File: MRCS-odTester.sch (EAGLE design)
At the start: 14 parts

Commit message: 1.1
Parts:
- added DCC, TRACK: (no value), SPCoast:CONNECTOR-M02508-LOCK
- R1: value 15k -> 100k
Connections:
- removed net TRACK+: DCCOD-2.S, SW1.S, SW1.S1, SW2.S, SW2.S1, SW3.S, SW3.S1
- removed net TRACK-: DCCOD-4.S, R1.1, R2.1, R3.1
- new net DCC-COMMON: DCC.2, DCCOD-4.S
- new net DCC-FROMTRACK: DCCOD-2.S, SW1.S, SW1.S1, SW2.S, SW2.S1, SW3.S, SW3.S1, TRACK.1
- new net DCC-TOTRACK: DCC.1, R1.1, R2.1, R3.1, TRACK.2
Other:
- moved on the sheet: C1, C2, CON1, DCCOD-1, DCCOD-2, DCCOD-3, DCCOD-4, DCCOD-5, LED1, R1, R2, R3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

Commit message: 2.0
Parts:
- BOARD1: value BOARD50X50 -> (none)
- C1: device SPCoast:CAP-POLPTH-5MM -> SPCoast:CAP-POLPTH-3.5MM
- R1, R2, R3, R4: device SPCoast:RPTH1 -> SPCoast:RPTH04
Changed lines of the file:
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@@
 <grid distance="0.1" unitdist="inch" unit="inch" style="lines" multiple="1" display="no" altdistance="0.01" altunitdist="inch" altunit="inch"/>
 <layers>
-<layer number="1" name="Top" color="4" fill="1" visible="no" active="no"/>
-<layer number="2" name="Route2" color="1" fill="3" visible="no" active="no"/>
-<layer number="3" name="Route3" color="4" fill="3" visible="no" active="no"/>
-<layer number="14" name="Route14" color="1" fill="6" visible="no" active="no"/>
-<layer number="15" name="Route15" color="4" fill="6" visible="no" active="no"/>
-<layer number="16" name="Bottom" color="2" fill="1" visible="no" active="no"/>
-<layer number="17" name="Pads" color="2" fill="1" visible="no" active="no"/>
-<layer number="18" name="Vias" color="2" fill="1" visible="no" active="no"/>
-<layer number="19" name="Unrouted" color="6" fill="1" visible="no" active="no"/>
-<layer number="20" name="Dimension" color="27" fill="1" visible="no" active="no"/>
-<layer number="21" name="tPlace" color="20" fill="1" visible="no" active="no"/>
-<layer number="22" name="bPlace" color="7" fill="1" visible="no" active="no"/>
-<layer number="23" name="tOrigins" color="15" fill="1" visible="no" active="no"/>
-<layer number="24" name="bOrigins" color="15" fill="1" visible="no" active="no"/>
-<layer number="25" name="tNames" color="7" fill="1" visible="no" active="no"/>
-<layer number="26" name="bNames" color="7" fill="1" visible="no" active="no"/>
-<layer number="27" name="tValues" color="7" fill="1" visible="no" active="no"/>
-<layer number="28" name="bValues" color="7" fill="1" visible="no" active="no"/>
+<layer number="1" name="Top" color="4" fill="1" visible="yes" active="no"/>
+<layer number="2" name="Route2" color="1" fill="3" visible="yes" active="no"/>
+<layer number="3" name="Route3" color="4" fill="3" visible="yes" active="no"/>
+<layer number="14" name="Route14" color="1" fill="6" visible="yes" active="no"/>
+<layer number="15" name="Route15" color="4" fill="6" visible="yes" active="no"/>
+<layer number="16" name="Bottom" color="1" fill="1" visible="yes" active="no"/>
+<layer number="17" name="Pads" color="2" fill="1" visible="yes" active="no"/>
+<layer number="18" name="Vias" color="2" fill="1" visible="yes" active="no"/>
+<layer number="19" name="Unrouted" color="6" fill="1" visible="yes" active="no"/>
+<layer number="20" name="Dimension" color="15" fill="1" visible="yes" active="no"/>
+<layer number="21" name="tPlace" color="7" fill="1" visible="yes" active="no"/>
+<layer number="22" name="bPlace" color="7" fill="1" visible="yes" active="no"/>
+<layer number="23" name="tOrigins" color="15" fill="1" visible="yes" active="no"/>
+<layer number="24" name="bOrigins" color="15" fill="1" visible="yes" active="no"/>
+<layer number="25" name="tNames" color="7" fill="1" visible="yes" active="no"/>
+<layer number="26" name="bNames" color="7" fill="1" visible="yes" active="no"/>
+<layer number="27" name="tValues" color="7" fill="1" visible="yes" active="no"/>
+<layer number="28" name="bValues" color="7" fill="1" visible="yes" active="no"/>
 <layer number="29" name="tStop" color="7" fill="3" visible="no" active="no"/>
 <layer number="30" name="bStop" color="7" fill="6" visible="no" active="no"/>
@@
 <layer number="35" name="tGlue" color="7" fill="4" visible="no" active="no"/>
 <layer number="36" name="bGlue" color="7" fill="5" visible="no" active="no"/>
-<layer number="37" name="tTest" color="7" fill="1" visible="no" active="no"/>
-<layer number="38" name="bTest" color="7" fill="1" visible="no" active="no"/>
+<layer number="37" name="tTest" color="7" fill="1" visible="yes" active="no"/>
+<layer number="38" name="bTest" color="7" fill="1" visible="yes" active="no"/>
 <layer number="39" name="tKeepout" color="4" fill="11" visible="no" active="no"/>
 <layer number="40" name="bKeepout" color="1" fill="11" visible="no" active="no"/>
@@
 <layer number="44" name="Drills" color="7" fill="1" visible="no" active="no"/>
 <layer number="45" name="Holes" color="7" fill="1" visible="no" active="no"/>
-<layer number="46" name="Milling" color="3" fill="1" visible="no" active="no"/>
-<layer number="47" name="Measures" color="7" fill="1" visible="no" active="no"/>
-<layer number="48" name="Document" color="7" fill="1" visible="no" active="no"/>
-<layer number="49" name="Reference" color="21" fill="1" visible="no" active="no"/>
-<layer number="50" name="dxf" color="7" fill="1" visible="no" active="no"/>
-<layer number="51" name="tDocu" color="16" fill="1" visible="no" active="no"/>
-<layer number="52" name="bDocu" color="31" fill="1" visible="no" active="no"/>
-<layer number="53" name="tGND_GNDA" color="7" fill="9" visible="no" active="no"/>
-<layer number="54" name="bGND_GNDA" color="1" fill="9" visible="no" active="no"/>
-<layer number="56" name="wert" color="7" fill="1" visible="no" active="no"/>
-<layer number="57" name="tCAD" color="7" fill="1" visible="no" active="no"/>
-<layer number="59" name="tCarbon" color="7" fill="1" visible="no" active="no"/>
-<layer number="60" name="bCarbon" color="7" fill="1" visible="no" active="no"/>
+<layer number="46" name="Milling" color="3" fill="1" visible="yes" active="no"/>
+<layer number="47" name="Measures" color="7" fill="1" visible="yes" active="no"/>
+<layer number="48" name="Document" color="7" fill="1" visible="yes" active="no"/>
+<layer number="49" name="Reference" color="7" fill="1" visible="yes" active="no"/>
+<layer number="50" name="dxf" color="7" fill="1" visible="yes" active="no"/>
+<layer number="51" name="tDocu" color="7" fill="1" visible="yes" active="no"/>
+<layer number="52" name="bDocu" color="7" fill="1" visible="yes" active="no"/>
+<layer number="53" name="tGND_GNDA" color="7" fill="9" visible="yes" active="no"/>
+<layer number="54" name="bGND_GNDA" color="1" fill="9" visible="yes" active="no"/>
+<layer number="56" name="wert" color="7" fill="1" visible="yes" active="no"/>
+<layer number="57" name="tCAD" color="7" fill="1" visible="yes" active="no"/>
+<layer number="59" name="tCarbon" color="7" fill="1" visible="yes" active="no"/>
+<layer number="60" name="bCarbon" color="7" fill="1" visible="yes" active="no"/>
 <layer number="90" name="Modules" color="5" fill="1" visible="yes" active="yes"/>
 <layer number="91" name="Nets" color="2" fill="1" visible="yes" active="yes"/>
@@
 <part name="FRAME1" library="SPCoast" deviceset="DOC-FRAME-LETTER" device=""/>
 <part name="DCCOD" library="con-molex" deviceset="KK-156-5" device=""/>
-<part name="C1" library="SPCoast" deviceset="CAP-POL*" device="PTH-5MM" value="100uF"/>
+<part name="C1" library="SPCoast" deviceset="CAP-POL*" device="PTH-3.5MM" value="100uF"/>
 <part name="C2" library="SPCoast" deviceset="CAP*" device="" value="0.1uf"/>
-<part name="R1" library="SPCoast" deviceset="R*" device="PTH1" value="100k"/>
-<part name="R2" library="SPCoast" deviceset="R*" device="PTH1" value="10k"/>
-<part name="R3" library="SPCoast" deviceset="R*" device="PTH1" value="5k"/>
+<part name="R1" library="SPCoast" deviceset="R*" device="PTH04" value="100k"/>
+<part name="R2" library="SPCoast" deviceset="R*" device="PTH04" value="10k"/>
+<part name="R3" library="SPCoast" deviceset="R*" device="PTH04" value="5k"/>
 <part name="SW1" library="SPCoast" deviceset="SWITCH-10-XX" device=""/>
 <part name="SW2" library="SPCoast" deviceset="SWITCH-10-XX" device=""/>
@@
 <part name="P+1" library="supply1" deviceset="+12V" device=""/>
 <part name="CON1" library="SPCoast" deviceset="CONNECTOR-DC-POWER" device="-RA"/>
-<part name="R4" library="SPCoast" deviceset="R*" device="PTH1" value="2k"/>
+<part name="R4" library="SPCoast" deviceset="R*" device="PTH04" value="2k"/>
 <part name="LED1" library="SPCoast" deviceset="LED*" device="LED5MM"/>
 <part name="P+3" library="supply1" deviceset="+12V" device=""/>

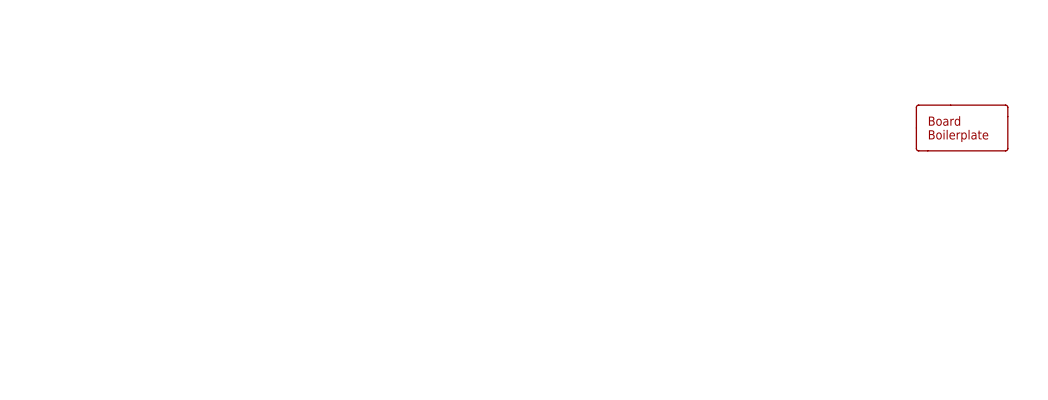
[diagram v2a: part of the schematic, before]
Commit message: silkscreen cleanup
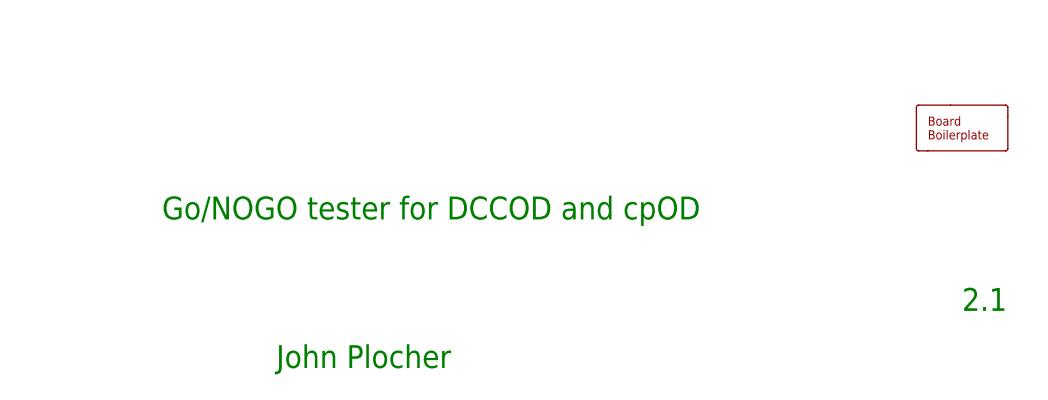
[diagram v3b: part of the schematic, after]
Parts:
- BOARD1: value (none) -> BOARD50X50
- C2: device SPCoast:CAP -> SPCoast:CAPPTH1
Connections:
- net DCC-COMMON: now also DCC.B; no longer DCC.2
- net DCC-FROMTRACK: now also TRACK.A; no longer TRACK.1
- net DCC-TOTRACK: now also DCC.A, TRACK.B; no longer DCC.1, TRACK.2
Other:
- note added: "2.1"
- note added: "Go/NOGO tester for DCCOD and cpOD"
- note added: "John Plocher"

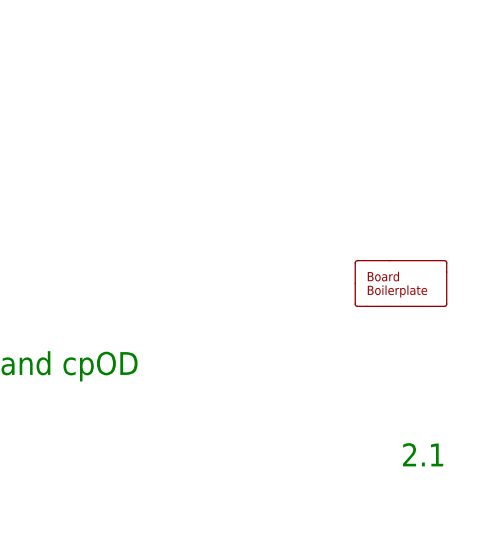
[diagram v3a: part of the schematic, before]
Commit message: created 2x2 panel
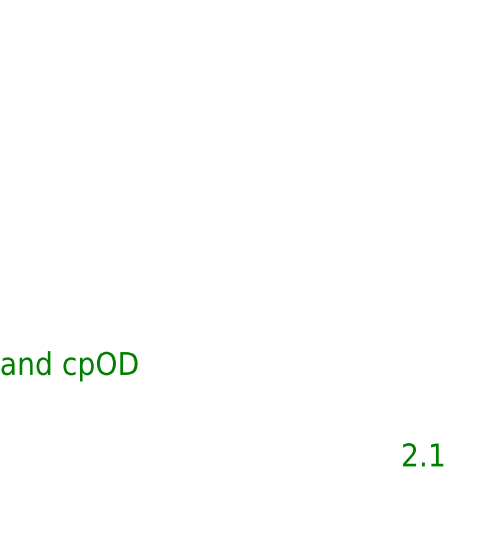
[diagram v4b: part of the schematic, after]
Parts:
- removed BOARD1: BOARD50X50, SPCoast:BOARD50X50
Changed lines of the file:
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@@
 <part name="P+4" library="supply1" deviceset="+12V" device=""/>
 <part name="GND3" library="supply1" deviceset="GND" device=""/>
-<part name="BOARD1" library="SPCoast" deviceset="BOARD" device="50X50"/>
 <part name="U$1" library="SPCoast" deviceset="DOC-POWER_LABEL" device="" value="+12v"/>
 <part name="DCC" library="SPCoast" deviceset="CONNECTOR-M02" device="508-LOCK"/>
@@
 <instance part="P+4" gate="1" x="101.6" y="78.74"/>
 <instance part="GND3" gate="1" x="101.6" y="55.88"/>
-<instance part="BOARD1" gate="B" x="241.3" y="33.02"/>
 <instance part="U$1" gate="PWR1" x="81.28" y="66.04"/>
 <instance part="DCC" gate="J" x="177.8" y="99.06" rot="R180"/>
@@
 </schematic>
 </drawing>
-<compatibility>
-<note version="6.3" minversion="6.2.2" severity="warning">
-Since Version 6.2.2 text objects can contain more than one line,
-which will not be processed correctly with this version.
-</note>
-</compatibility>
 </eagle>
